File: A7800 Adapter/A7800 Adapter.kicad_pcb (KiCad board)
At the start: 2 copper layers, 29.2 x 31.8 mm, 10 parts, among them J1 JoyKEY, J2 Atari 7800, Q1 2N3906, Q2 2N3906

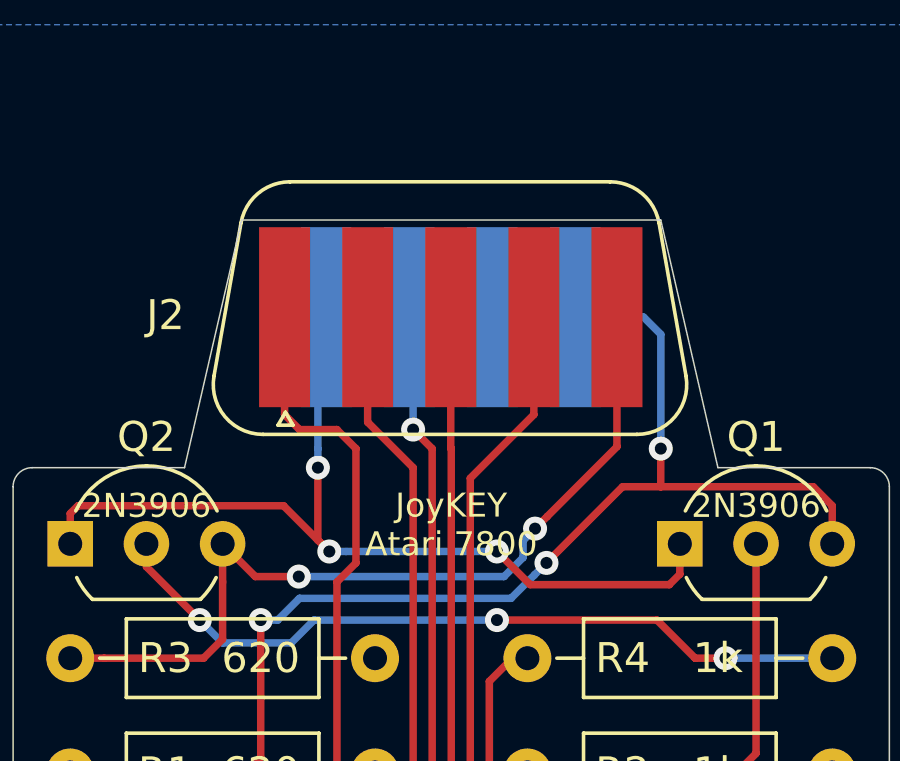
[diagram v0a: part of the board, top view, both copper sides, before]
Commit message: Updated A7800 silkscreen
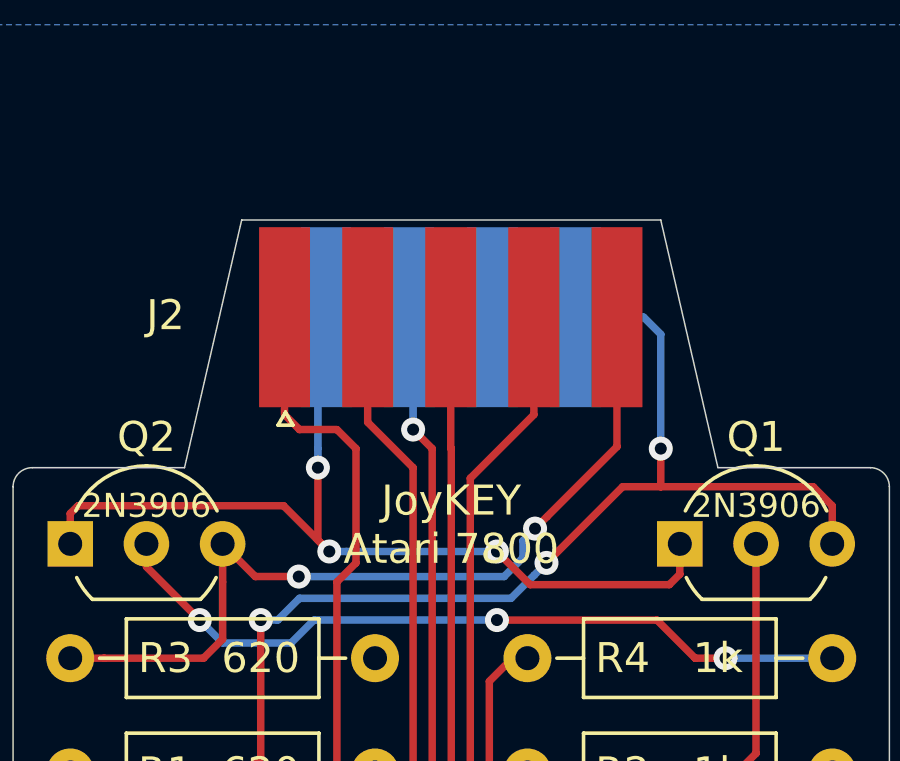
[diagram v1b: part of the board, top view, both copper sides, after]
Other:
- rule pad_to_mask_clearance: 0.051 -> 0
- board text added: "Atari 7800 Pro System"
